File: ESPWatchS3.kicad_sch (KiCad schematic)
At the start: 113 parts, among them J1 OLED, J2 USB, J3 UART0, U1 ESP32-S3R8, U10 BD48KxxG, U2 EVA-M8Q-0, U3 BME280, U4 IS25LP128F-JKLE, U5 BQ27441-G1A, U6 BQ24075RGTR, U7 TPS631000DRLR, U8 AP3012, U9 NJG1143UA2-TE1, Y1 40MHz, Y2 32.768kHz, Y3 32.768kHz

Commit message: PCB Work
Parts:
- removed H1, H2, H3, H4: MountingHole_Pad, MountingHole:MountingHole_2.2mm_M2_Pad, symbol Mechanical:MountingHole_Pad
- added H1, H2, H3, H4: MountingHole, MountingHole:MountingHole_2.2mm_M2, symbol Mechanical:MountingHole

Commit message: Schematic work
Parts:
- removed R4: 100k, Resistor_SMD:R_0402_1005Metric, symbol Device:R_Small
- added C46: 1u, Capacitor_SMD:C_0402_1005Metric, symbol Device:C_Small
- added TP1: GNSS Reset, symbol Connector:TestPoint
- R2: value 100k -> 499k
- R25: value 9.1k -> 47.5k
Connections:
- net +3V3: no longer J1.5 (Pin_5), R9.2
- net EP: now also R9.1, C46.2; no longer C33.2, S4.2
- net USER_BTN4: no longer C33.1, R9.1, S4.1
- net at U2.14 (RESET_N): now also TP1.1
- net CHG_PWRGD: no longer names the net of U6.7 (~{PGOOD})
- net CHG_PWRGD: no longer U1.10 (GPIO5)
- new net: C33.1, S4.1
- new net: C46.1, J1.5 (Pin_5)
- new net PWR_BTN4: C33.2, R9.2, S4.2
- new net TPS_EN: U1.10 (GPIO5)
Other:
- moved on the sheet: C19, C33, C7, C8, C9, R9, S4

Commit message: Library and schematic cleanup, revised designwork
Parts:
- removed ANT2: 1575AT43A0040E, WatchParts:1575AT43A0040E, symbol WatchParts:1575AT43A0040E
- removed C10, C8, C9: 4.7u, Capacitor_SMD:C_0603_1608Metric, symbol Device:C_Small
- removed C12, C15, C19, C46: 1u, Capacitor_SMD:C_0402_1005Metric, symbol Device:C_Small
- removed C3: 10u, Capacitor_SMD:C_0402_1005Metric, symbol Device:C_Small
- removed C44: 2p, Capacitor_SMD:C_0402_1005Metric, symbol Device:C_Small
- removed C45: 0.001u, Capacitor_SMD:C_0402_1005Metric, symbol Device:C_Small
- removed D1: MBR0530, Diode_SMD:D_SOD-123, symbol Diode:MBR0530
- removed FL1: B39162B4327P810, WatchParts:FIL_B39162B4327P810, symbol WatchParts:B39162B4327P810
- removed J1: OLED, WatchParts:CS050Z24GA0, symbol Connector_Generic:Conn_01x24
- removed L3: 10u, Inductor_SMD:L_1008_2520Metric, symbol Device:L_Small
- removed L6: 9.1n, Inductor_SMD:L_0402_1005Metric, symbol Device:L_Small
- removed R1, R14, R5: 100k, Resistor_SMD:R_0402_1005Metric, symbol Device:R_Small
- removed R2: 499k, Resistor_SMD:R_0402_1005Metric, symbol Device:R_Small
- removed R25: 47.5k, Resistor_SMD:R_0402_1005Metric, symbol Device:R_Small
- removed R32: 1M, Resistor_SMD:R_0402_1005Metric, symbol Device:R_Small
- removed U2: EVA-M8Q-0, WatchParts:LGA43R65P9X9_700X700X116, symbol WatchParts:EVA-M8Q-0
- removed U3: BME280, Package_LGA:Bosch_LGA-8_2.5x2.5mm_P0.65mm_ClockwisePinNumbering, symbol Sensor:BME280
- removed U8: AP3012, Package_TO_SOT_SMD:SOT-23-5, symbol Regulator_Switching:AP3012
- removed U9: NJG1143UA2-TE1, WatchParts:AMP_NJG1143UA2-TE1, symbol WatchParts:NJG1143UA2-TE1
- added C?: 1u, Capacitor_SMD:C_0402_1005Metric, symbol Device:C_Small
- added C?: 0.1u, Capacitor_SMD:C_0402_1005Metric, symbol Device:C_Small
- added D2: Charge, symbol Device:LED_Small
- added J1: LCD, symbol Connector_Generic:Conn_01x18
- added R4: 1k, Resistor_SMD:R_0402_1005Metric, symbol Device:R_Small
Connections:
- net +3V3: now also C?.1, C?.1, J1.16 (Pin_16), J1.6 (Pin_6), J1.7 (Pin_7)
- net +SYS: now also R4.2; no longer U7.5 (EN)
- net CHG_EN1: now also U1.12 (GPIO7); no longer U1.11 (GPIO6)
- net CHG_EN2: now also U1.13 (GPIO8); no longer U1.12 (GPIO7)
- net EP: now also C?.2, C?.2, J1.14 (Pin_14), J1.18 (Pin_18), J1.5 (Pin_5), J1.8 (Pin_8)
- net ESP_RESET: now also J1.15 (Pin_15)
- net TPS_EN: now also U7.5 (EN); no longer U1.10 (GPIO5)
- net TPS_MODE: no longer U1.13 (GPIO8)
- net AP_EN: no longer names the net of U1.14 (GPIO9)
- net CHG_CHG: no longer names the net of U6.9 (~{CHG})
- net CHG_CHG: now also D2.1 (K); no longer U1.9 (GPIO4)
- net OLED_CS renamed LCD_CS
- net LCD_CS: now also J1.13 (Pin_13)
- net OLED_D/C renamed LCD_DC
- net LCD_DC: now also J1.12 (Pin_12)
- net OLED_MOSI renamed LCD_MOSI
- net LCD_MOSI: now also J1.10 (Pin_10)
- net OLED_RST: no longer names the net of U1.19 (GPIO14)
- net OLED_SCK renamed LCD_SCK
- net LCD_SCK: now also J1.9 (Pin_9)
- new net: D2.2 (A), R4.1
- new net LCD_TE: J1.17 (Pin_17)
- new net SMPS_EN: U1.10 (GPIO5)
- new net SMPS_MODE: U1.11 (GPIO6)
- no-connect marks 32 -> 19
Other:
- note added: "LCD Connector"
- note removed: "OLED Bias Supply"
- note removed: "OLED Connector"
- moved on the sheet: C1, C2, C24, C25, C29, C33, C6, L4, R10, R3, R30, R31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

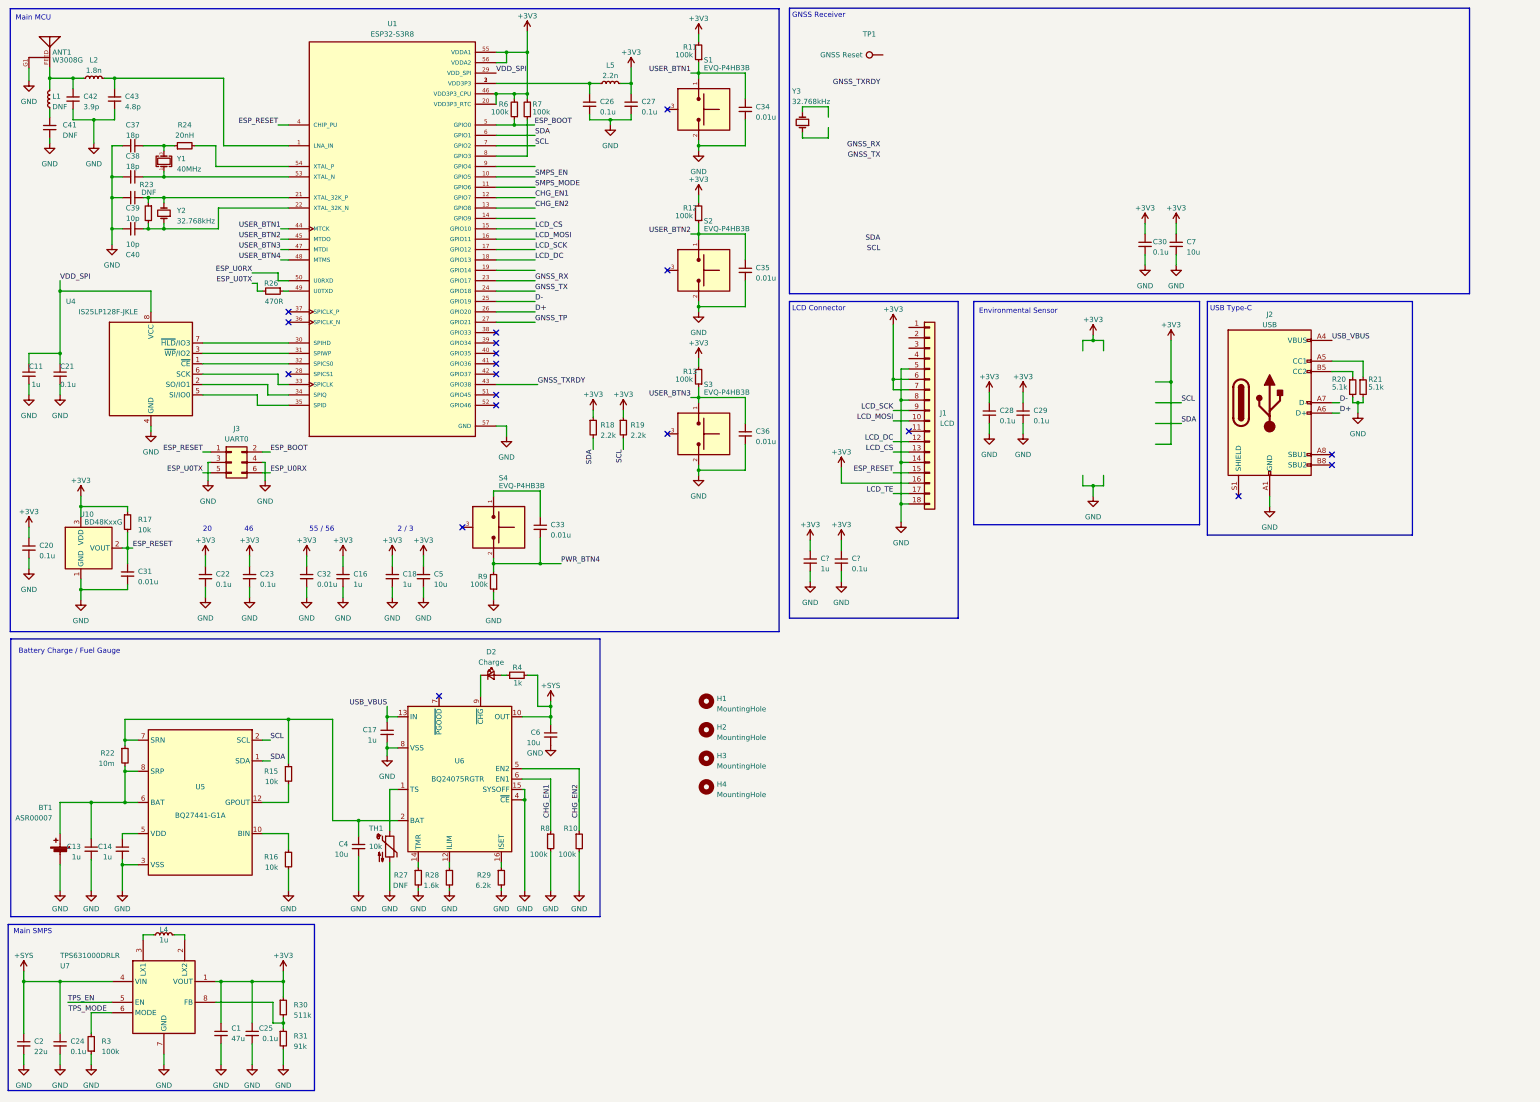
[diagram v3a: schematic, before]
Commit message: Finish and reannotate schematic minus LCD BL SMPS
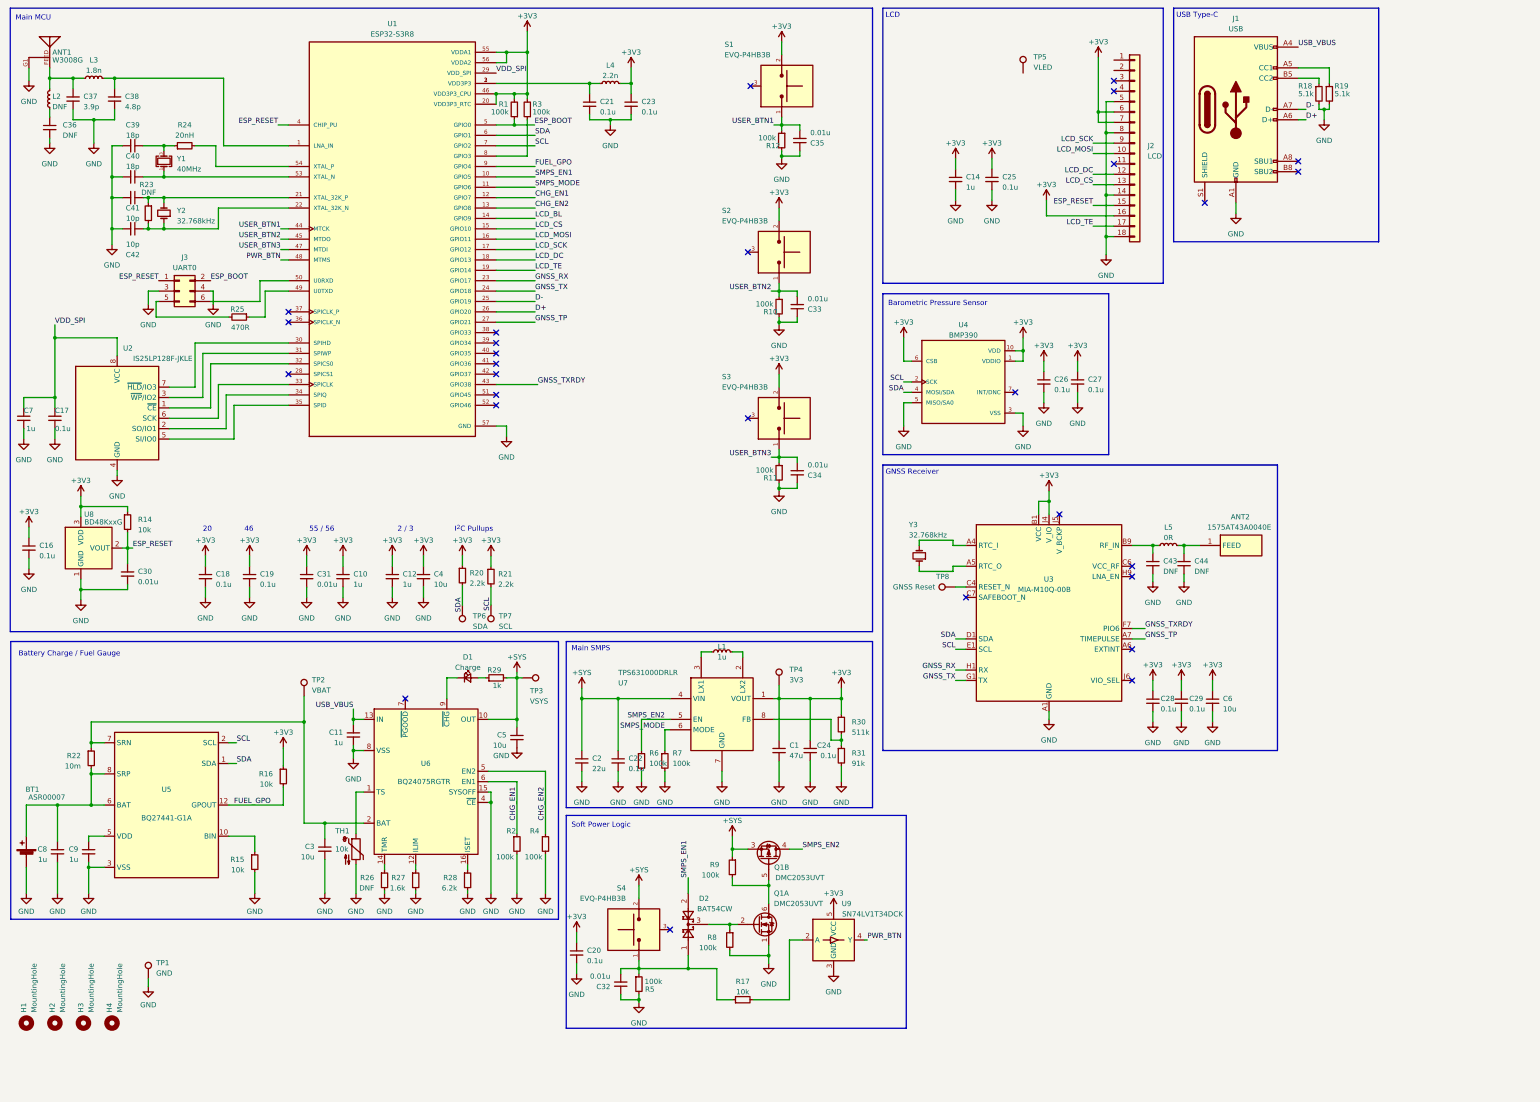
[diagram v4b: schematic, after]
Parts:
- removed C35, C36: 0.01u, Capacitor_SMD:C_0402_1005Metric, symbol Device:C_Small
- removed R12, R13, R3: 100k, Resistor_SMD:R_0402_1005Metric, symbol Device:R_Small
- added ANT2: 1575AT43A0040E, WatchParts:1575AT43A0040E, symbol WatchParts:1575AT43A0040E
- added C20, C28: 0.1u, Capacitor_SMD:C_0402_1005Metric, symbol Device:C_Small
- added C32, C34: 0.01u, Capacitor_SMD:C_0402_1005Metric, symbol Device:C_Small
- added C43, C44: DNF, Capacitor_SMD:C_0402_1005Metric, symbol Device:C_Small
- added D2: BAT54CW, Package_TO_SOT_SMD:SOT-323_SC-70, symbol Diode:BAT54CW
- added L5: 0R, Resistor_SMD:R_0402_1005Metric, symbol Device:L_Small
- added Q1: DMC2053UVT, Package_TO_SOT_SMD:SOT-363_SC-70-6, symbol WatchParts:DMC2710UDW
- added R10, R11, R5, R6, R7, R8: 100k, Resistor_SMD:R_0402_1005Metric, symbol Device:R_Small
- added R17: 10k, Resistor_SMD:R_0402_1005Metric, symbol Device:R_Small
- added TP1: GND, TestPoint:TestPoint_Pad_D1.0mm, symbol Connector:TestPoint
- added TP2: VBAT, TestPoint:TestPoint_Pad_D1.0mm, symbol Connector:TestPoint
- added TP3: VSYS, TestPoint:TestPoint_Pad_D1.0mm, symbol Connector:TestPoint
- added TP4: 3V3, TestPoint:TestPoint_Pad_D1.0mm, symbol Connector:TestPoint
- added TP5: VLED, TestPoint:TestPoint_Pad_D1.0mm, symbol Connector:TestPoint
- added TP6: SDA, TestPoint:TestPoint_Pad_D1.0mm, symbol Connector:TestPoint
- added TP7: SCL, TestPoint:TestPoint_Pad_D1.0mm, symbol Connector:TestPoint
- added U3: MIA-M10Q-00B, WatchParts:MIAM10Q00B, symbol WatchParts:MIA-M10Q-00B
- added U4: BMP390, WatchParts:XDCR_BMP390, symbol WatchParts:BMP390
- added U9: SN74LV1T34DCK, Package_TO_SOT_SMD:SOT-353_SC-70-5, symbol Logic_LevelTranslator:SN74LV1T34DCK
- D1: renamed from D2; footprint (none) -> LED_SMD:LED_0603_1608Metric
- TP8: renamed from TP1; footprint (none) -> TestPoint:TestPoint_Pad_D1.0mm
- U5: footprint Package_SON:Texas_S-PDSO-N12 -> WatchParts:Texas_S-PDSO-N12
- gave numbers to parts that had none: 2
- renumbered C16 to C10, C17 to C11, C18 to C12, C20 to C16, C21 to C17, C22 to C18, C23 to C19, C26 to C21, C24 to C22, C27 to C23, C25 to C24, C28 to C26, C29 to C27, C30 to C29, C4 to C3, C31 to C30, C32 to C31, C34 to C35, C41 to C36, C42 to C37, C43 to C38, C37 to C39, C5 to C4, C38 to C40, C39 to C41, C40 to C42, C6 to C5, C7 to C6, C11 to C7, C13 to C8, C14 to C9, J2 to J1, J1 to J2, L4 to L1, L1 to L2, L2 to L3, L5 to L4, R6 to R1, R11 to R12, R17 to R14, R16 to R15, R15 to R16, R20 to R18, R21 to R19, R8 to R2, R18 to R20, R19 to R21, R26 to R25, R27 to R26, R28 to R27, R29 to R28, R4 to R29, R7 to R3, R10 to R4, U4 to U2, U10 to U8
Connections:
- net TPS_MODE is gone; now on net SMPS_MODE: U7.6 (MODE)
- net +3V3: now also R16.1, S1.2, S2.2, S3.2, C20.1, C28.1, TP4.1, U3.B1 (VCC), U3.J4 (V_IO), U4.1 (VDDIO), U4.10 (VDD), U4.6 (CSB), U9.5 (VCC); no longer R12.2
- net +SYS: now also R9.1, S4.2, Q1.3 (S), TP3.1
- net BAT: now also TP2.1; no longer R16.1
- net EP: now also C33.1, C35.1, R12.2, C20.2, C28.2, C32.1, C34.1, C43.2, C44.2, Q1.1 (S), R10.2, R11.2, R5.2, R6.2, R7.2, R8.2, TP1.1, U3.A1 (GND), U3.A2 (GND), U3.A3 (GND), U3.A8 (GND), U3.A9 (GND), U3.B2 (GND), U3.B8 (GND), U3.C3 (GND), U3.C9 (GND), U3.E3 (GND), U3.E4 (GND), U3.E9 (GND), U3.F1 (GND), U3.F3 (GND), U3.F4 (GND), U3.G3 (GND), U3.G4 (GND), U3.G5 (GND), U3.G6 (GND), U3.H8 (GND), U3.J8 (GND), U3.J9 (GND), U4.3 (VSS), U4.5 (MISO/SA0), U4.8 (VSS), U4.9 (VSS), U9.3 (GND); no longer C35.2, R9.1, S1.2, S2.2, S3.2
- net GNSS_RX: now also U3.H1 (RX)
- net GNSS_TP: now also U3.A7 (TIMEPULSE)
- net GNSS_TX: now also U3.G1 (TX)
- net GNSS_TXRDY: now also U3.F7 (PIO6)
- net LCD_TE: now also U1.19 (GPIO14)
- net SCL: now also TP7.1, U3.E1 (SCL), U4.2 (SCK)
- net SDA: now also TP6.1, U3.D1 (SDA), U4.4 (MOSI/SDA)
- net SMPS_MODE: now also R7.1
- net USER_BTN1: now also C35.2; no longer C35.1
- net USER_BTN2: now also C33.2, R10.1
- net USER_BTN3: now also C34.2, R11.1
- net FUEL_GPO: now reaches R16.2, U5.12 (GPOUT)
- net FUEL_GPO: now also U1.9 (GPIO4)
- net at S4.1: now also C32.2, D2.1, R17.1, R5.1; no longer C33.1
- net LCD_BL: now reaches U1.14 (GPIO9)
- net at Y3.1: now also U3.A5 (RTC_O)
- net at Y3.2: now also U3.A4 (RTC_I)
- net at TP8.1: now also U3.C4 (RESET_N)
- net ESP_U0RX: no longer names the net of J3.6 (Pin_6), U1.50 (U0RXD)
- net ESP_U0TX: no longer names the net of J3.5 (Pin_5), R25.2
- removed net PWR_BTN4: C33.2, R9.2, S4.2
- net SMPS_EN renamed SMPS_EN1
- net SMPS_EN1: now also D2.2
- net TPS_EN renamed SMPS_EN2
- net SMPS_EN2: now also Q1.4 (D), R6.1
- net USER_BTN4 renamed PWR_BTN
- net PWR_BTN: now also U9.4 (Y)
- new net: D2.3, Q1.2 (G), R8.1
- new net: C43.1, L5.1, U3.B9 (RF_IN)
- new net: U3.C1 (RESERVED), U3.C5 (RESERVED), U3.D2 (RESERVED), U3.D9 (RESERVED), U3.E2 (RESERVED), U3.E7 (RESERVED), U3.F9 (RESERVED), U3.G7 (RESERVED), U3.G9 (RESERVED), U3.J1 (RESERVED), U3.J2 (RESERVED), U3.J3 (RESERVED), U3.J7 (RESERVED)
- new net: Q1.5 (G), Q1.6 (D), R9.2
- new net: ANT2.1 (FEED), C44.1, L5.2
- new net: R17.2, U9.2 (A)
- no-connect marks 19 -> 28
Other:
- note added: "Barometric Pressure Sensor"
- note added: "I^{2}C Pullups"
- note added: "LCD"
- note added: "Soft Power Logic"
- note removed: "Environmental Sensor"
- note removed: "LCD Connector"
- moved on the sheet: BT1, C1, C11, C14, C17, C2, C22, C24, C25, C26, C27, C29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

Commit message: Rethought pin allocation for power use
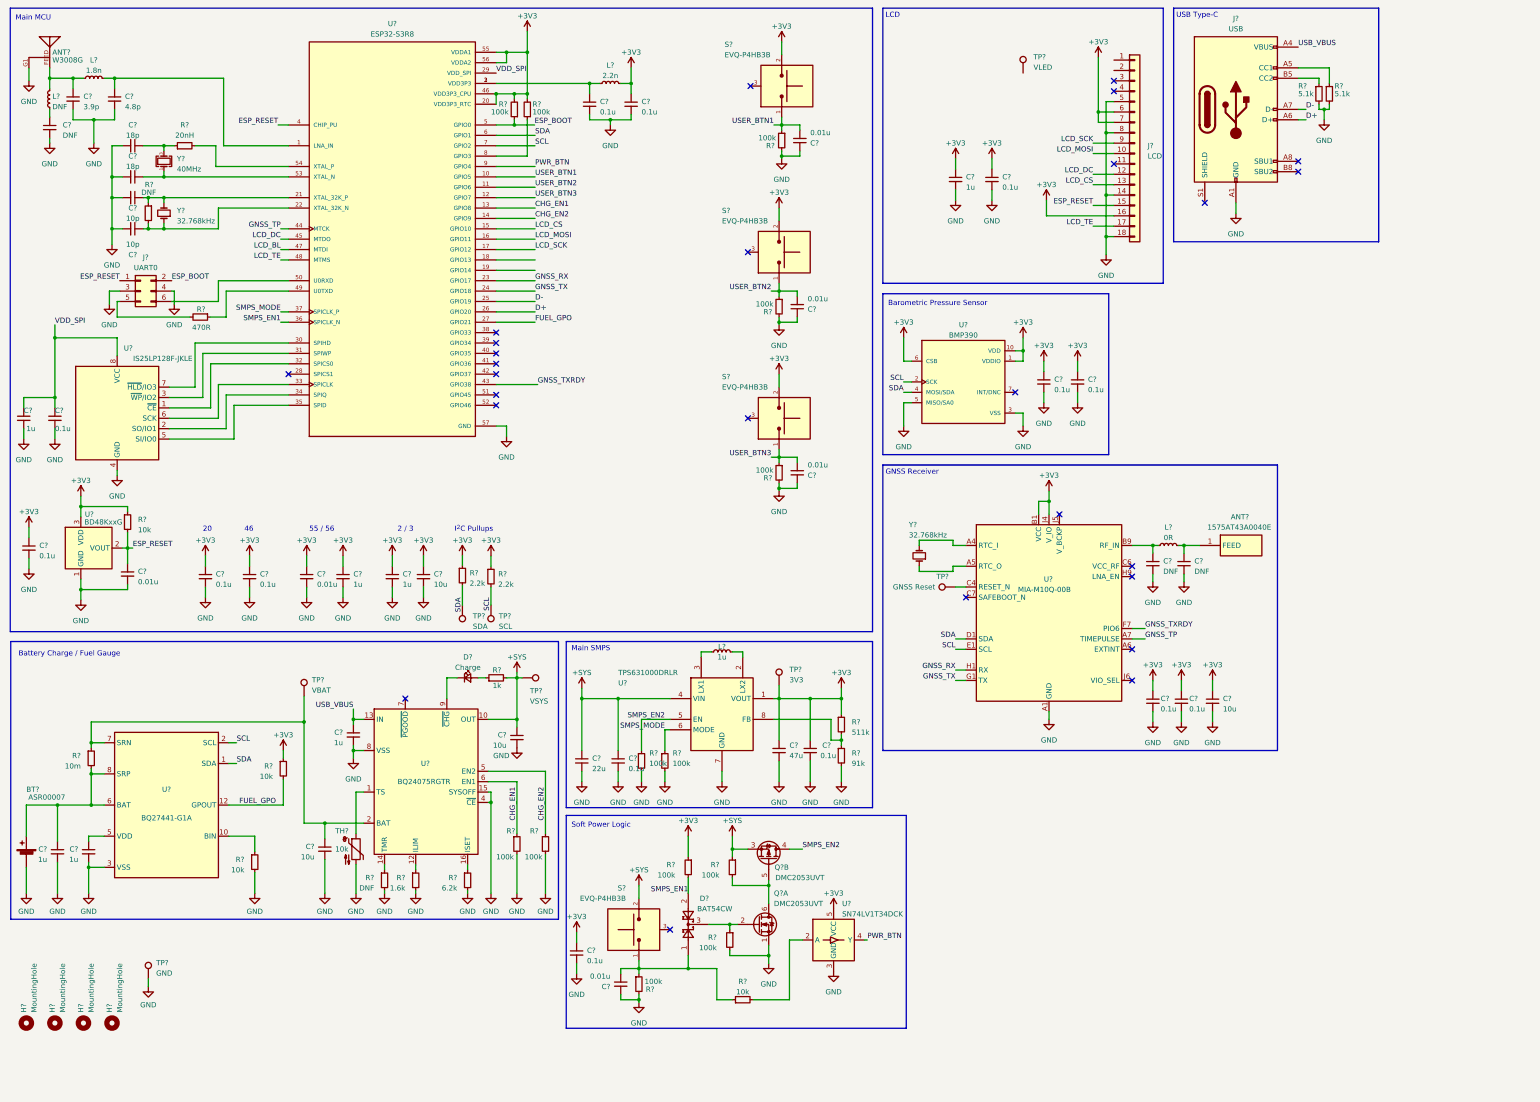
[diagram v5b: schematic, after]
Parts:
- removed R16: 10k, Resistor_SMD:R_0402_1005Metric, symbol Device:R_Small
- added R?: 100k, Resistor_SMD:R_0402_1005Metric, symbol Device:R_Small
- added R?: 10k, Resistor_SMD:R_0402_1005Metric, symbol Device:R_Small
- renumbered ANT1 to ANT?, ANT2 to ANT?, BT1 to BT?, C38 to C?, C12 to C?, C24 to C?, C33 to C?, C42 to C?, C21 to C?, C2 to C?, C40 to C?, C8 to C?, C22 to C?, C16 to C?, C20 to C?, C11 to C?, C14 to C?, C43 to C?, C9 to C?, C23 to C?, C10 to C?, C34 to C?, C36 to C?, C5 to C?, C19 to C?, C37 to C?, C27 to C?, C4 to C?, C26 to C?, C1 to C?, C28 to C?, C3 to C?, C18 to C?, C25 to C?, C6 to C?, C31 to C?, C35 to C?, C7 to C?, C29 to C?, C32 to C?, C41 to C?, C39 to C?, C44 to C?, C30 to C?, C17 to C?, D1 to D?, D2 to D?, H1 to H?, H3 to H?, H4 to H?, H2 to H?, J2 to J?, J3 to J?, J1 to J?, L2 to L?, L1 to L?, L5 to L?, L3 to L?, L4 to L?, Q1 to Q?, R11 to R?, R8 to R?, R14 to R?, R22 to R?, R21 to R?, R18 to R?, R28 to R?, R1 to R?, R24 to R?, R15 to R?, R4 to R?, R9 to R?, R27 to R?, R5 to R?, R3 to R?, R20 to R?, R30 to R?, R17 to R?, R7 to R?, R23 to R?, R29 to R?, R2 to R?, R31 to R?, R10 to R?, R19 to R?, R26 to R?, R12 to R?, R6 to R?, R25 to R?, S4 to S?, S1 to S?, S3 to S?, S2 to S?, TH1 to TH?, TP5 to TP?, TP2 to TP?, TP8 to TP?, TP3 to TP?, TP1 to TP?, TP4 to TP?, TP7 to TP?, TP6 to TP?, U3 to U?, U1 to U?, U4 to U?, U9 to U?, U5 to U?, U7 to U?, U8 to U?, U2 to U?, U6 to U?, Y1 to Y?, Y3 to Y?, Y2 to Y?
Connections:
- net +3V3: now also R?.1, R?.1
- net CHG_EN1: now also U?.13 (GPIO8); no longer U?.12 (GPIO7)
- net CHG_EN2: now also U?.14 (GPIO9); no longer U?.13 (GPIO8)
- net FUEL_GPO: now also U?.27 (GPIO21), R?.2; no longer U?.9 (GPIO4)
- net GNSS_TP: now also U?.44 (MTCK); no longer U?.27 (GPIO21)
- net LCD_BL: now also U?.47 (MTDI); no longer U?.14 (GPIO9)
- net LCD_DC: now also U?.45 (MTDO); no longer U?.18 (GPIO13)
- net LCD_TE: now also U?.48 (MTMS); no longer U?.19 (GPIO14)
- net PWR_BTN: now also U?.9 (GPIO4); no longer U?.48 (MTMS)
- net SMPS_EN1: now also U?.36 (SPICLK_N), R?.2; no longer U?.10 (GPIO5)
- net SMPS_MODE: now also U?.37 (SPICLK_P); no longer U?.11 (GPIO6)
- net USER_BTN1: now also U?.10 (GPIO5); no longer U?.44 (MTCK)
- net USER_BTN2: now also U?.11 (GPIO6); no longer U?.45 (MTDO)
- net USER_BTN3: now also U?.12 (GPIO7); no longer U?.47 (MTDI)
- no-connect marks 28 -> 26
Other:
- moved on the sheet: J?, R?

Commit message: Finalize schematic?
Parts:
- added C? (x2): 0.1u, Capacitor_SMD:C_0402_1005Metric, symbol Device:C_Small
- added C? (x2): 10u, Capacitor_SMD:C_0402_1005Metric, symbol Device:C_Small
- added C?: 1u, Capacitor_SMD:C_0402_1005Metric, symbol Device:C_Small
- added D?: CDSQR400B, Diode_SMD:D_SOD-923, symbol WatchParts:CDSQR400B
- added L?: 22u, symbol Device:L_Small
- added R?: 10R, Resistor_SMD:R_0402_1005Metric, symbol Device:R_Small
- added R?: 100k, Resistor_SMD:R_0402_1005Metric, symbol Device:R_Small
- added U?: AP3036B, Package_TO_SOT_SMD:SOT-23-6, symbol WatchParts:AP3036B
- added U?: ICM-42688-P, WatchParts:PQFN50P300X250X97-14N, symbol WatchParts:ICM-42688-P
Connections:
- net +3V3: now also C?.1, C?.1, C?.1, C?.1, L?.1, U?.1 (AP_AD0), U?.12 (AP_CS), U?.3 (VIN), U?.5 (VDDIO), U?.8 (VDD)
- net EP: now also C?.2, C?.2, C?.2, C?.2, C?.2, R?.2, R?.2, U?.5 (GND), U?.6 (GND), U?.7 (RESV)
- net LCD_BL: now also R?.1, U?.1 (CTRL)
- net SCL: now also U?.13 (AP_SCL)
- net SDA: now also U?.14 (AP_SDA)
- net at TP?.1: now also J?.2 (Pin_2), C?.1, U?.2 (VOUT)
- net at J?.1 (Pin_1): now also D?. (K)
- net IMU_INT1: now reaches U?.18 (GPIO13)
- net IMU_INT1: now also U?.4 (INT1)
- net IMU_INT2: now reaches U?.19 (GPIO14)
- net IMU_INT2: now also U?.9 (INT2)
- new net: L?.2, U?.4 (SW)
- new net: D?. (K), R?.1, U?.6 (FB)
- new net: U?.10 (RESV_10), U?.11 (RESV_11), U?.2 (RESV_2), U?.3 (RESV_3)
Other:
- note added: "IMU"
- moved on the sheet: C?, TP?

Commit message: Re-annotated schematic
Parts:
- R28: renamed from R?; value 1k -> 470R
- gave numbers to parts that had none: 126
